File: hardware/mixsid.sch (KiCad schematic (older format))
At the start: 69 parts, among them P1 INPUT, P2 CONTROL, P4 SOCKET LEFT, P5 OUTPUT, P6 SOCKET RIGHT, Q1 BC547, Q2 BC547, U1 GAL16V8, U2 SID2, U3 7812, U4 7809, U5 SID1, U6 4052, U7 4053, U8 ICL7660

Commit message: Hardware: Replaced balance pots with round types (bourns 3339), rearranged
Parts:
- RV3, RV4: footprint Potentiometers:Potentiometer_Bourns_3296W_3-8Zoll_Inline_ScrewUp -> Potentiometers:Potentiometer_Bourns_3339P_Angular_ScrewUp
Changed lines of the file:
@@
 F 0 "RV3" H 4100 4200 50  0000 C CNN
 F 1 "10k" H 4100 4300 50  0000 C CNN
-F 2 "Potentiometers:Potentiometer_Bourns_3296W_3-8Zoll_Inline_ScrewUp" H 4100 4300 60  0001 C CNN
+F 2 "Potentiometers:Potentiometer_Bourns_3339P_Angular_ScrewUp" H 4100 4300 60  0001 C CNN
 F 3 "" H 4100 4300 60  0000 C CNN
 	1    4100 4300
@@
 F 0 "RV4" H 7050 4250 50  0000 C CNN
 F 1 "10k" H 7050 4350 50  0000 C CNN
-F 2 "Potentiometers:Potentiometer_Bourns_3296W_3-8Zoll_Inline_ScrewUp" H 7050 4350 60  0001 C CNN
+F 2 "Potentiometers:Potentiometer_Bourns_3339P_Angular_ScrewUp" H 7050 4350 60  0001 C CNN
 F 3 "" H 7050 4350 60  0000 C CNN
 	1    7050 4350

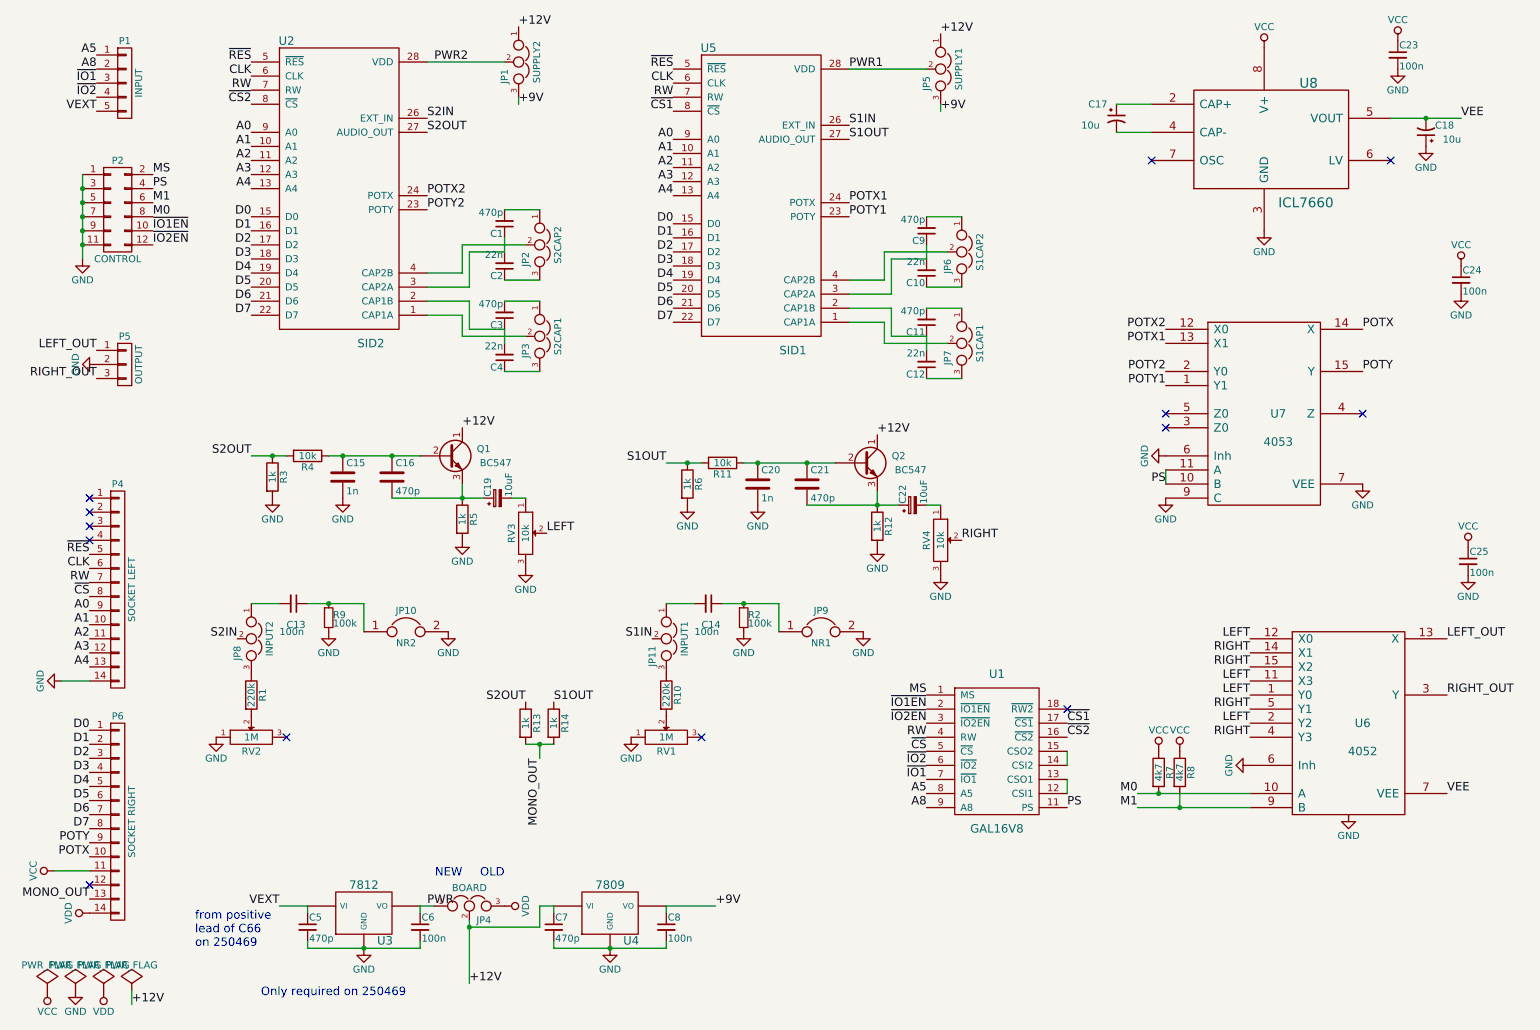
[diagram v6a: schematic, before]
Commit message: Firmware/Hardware: RW2 signal controls SID2 RW during parallel addressing
Depending on RW2, SID2 is write-only or read-write when addressed alongside
SID1.

The default setting is write-only to assure proper paddle support.
For mono tunes that use the readable registers for special effects,
parallel addressing would result in only one SID playing those effects
properly, thus RW2 allows the user to make both sids read-write.
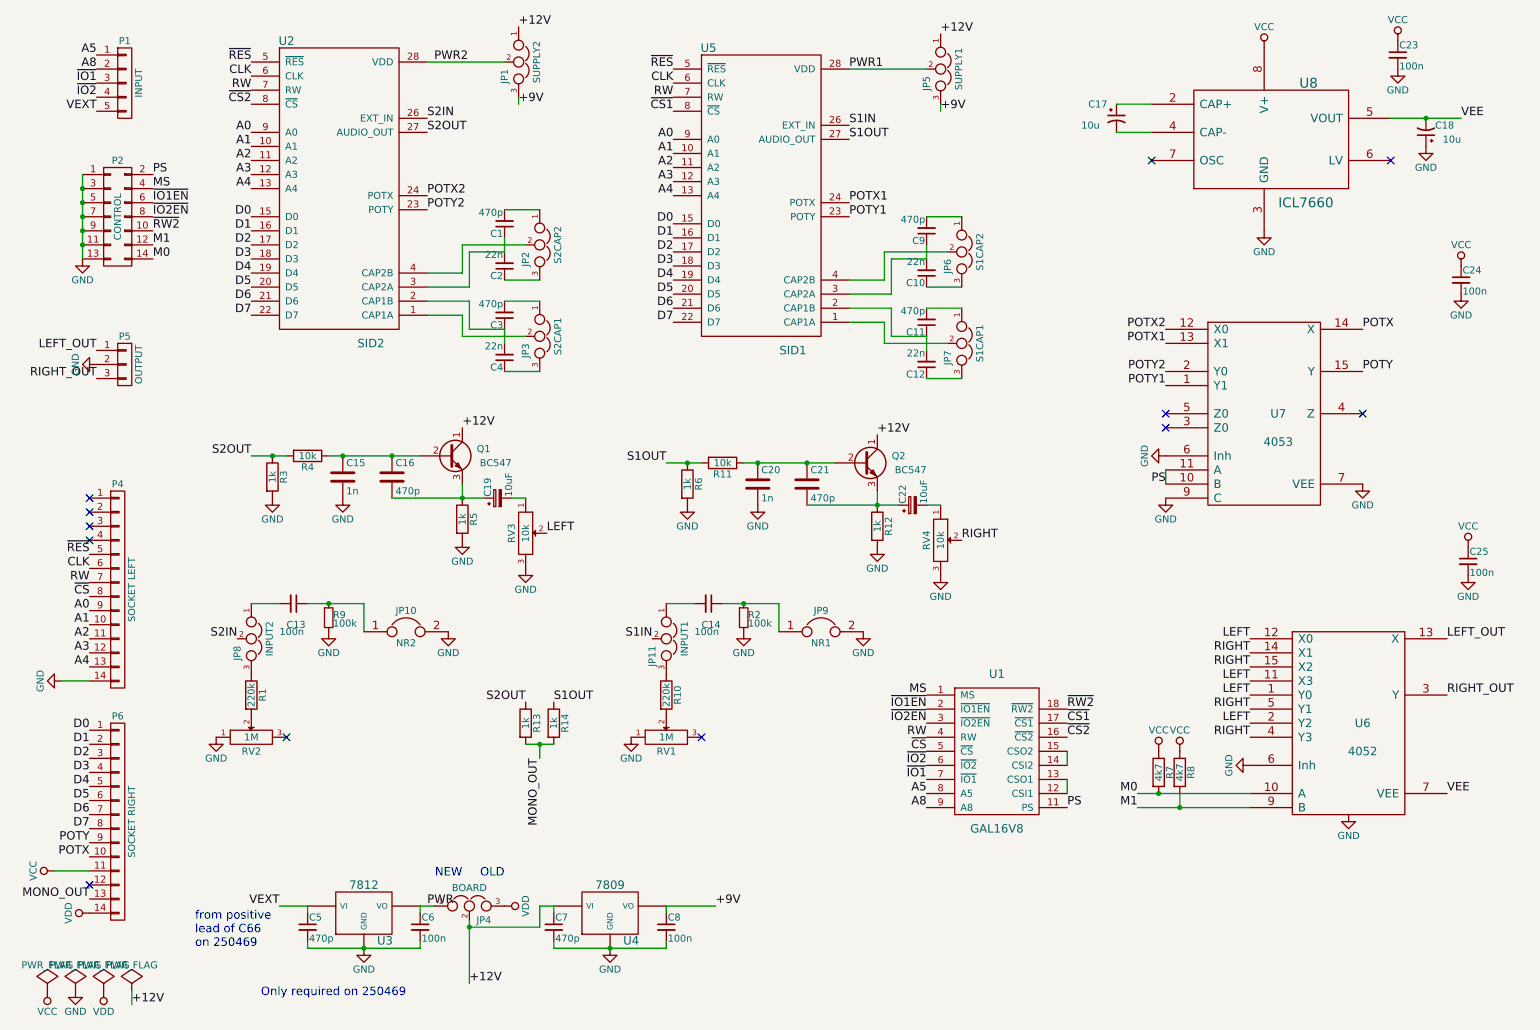
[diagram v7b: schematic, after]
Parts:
- removed P2: CONTROL, Pinheaders:Pin_Header_Straight_2x06, symbol CONN_02X06
- added P2: CONTROL, Pin_Headers:Pin_Header_Straight_2x07, symbol CONN_02X07
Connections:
- net GND: now also P2.1 (P1), P2.11 (P11), P2.13 (P13), P2.3 (P3), P2.5 (P5), P2.7 (P7), P2.9 (P9)
- net M0: now also P2.14 (P14)
- net M1: now also P2.12 (P12)
- net MS: now also P2.4 (P4)
- net PS: now also P2.2 (P2)
- net ~IO1EN: now also P2.6 (P6)
- net ~IO2EN: now also P2.8 (P8)
- net ~RW2: now reaches U1.18 (~RW2)
- net ~RW2: now also P2.10 (P10)
- no-connect marks 13 -> 12
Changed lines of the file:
@@
 Text Label 6950 5550 2    60   ~ 0
 ~IO1EN
-Text Label 1450 1750 0    60   ~ 0
+Text Label 1450 1850 0    60   ~ 0
 MS
-Text Label 1450 2150 0    60   ~ 0
+Text Label 1450 1950 0    60   ~ 0
 ~IO1EN
 $Comp
@@
 Text Label 10650 5450 0    60   ~ 0
 RIGHT_OUT
-Text Label 1450 2050 0    60   ~ 0
+Text Label 1450 2350 0    60   ~ 0
 M0
-Text Label 1450 1950 0    60   ~ 0
+Text Label 1450 2250 0    60   ~ 0
 M1
 Text Notes 3250 7600 2    60   ~ 0
@@
 Wire Wire Line
 	4200 6950 4300 6950
-Text Label 1450 2250 0    60   ~ 0
+Text Label 1450 2050 0    60   ~ 0
 ~IO2EN
 Text Label 6950 5650 2    60   ~ 0
@@
 	1    0    0    -1
 $EndComp
-NoConn ~ 7950 5550
 Text Label 7950 6250 0    60   ~ 0
 PS
@@
 Wire Wire Line
 	7950 5950 7950 5850
-$Comp
-L CONN_02X06 P2
-U 1 1 57221CBF
-P 1200 2000
-F 0 "P2" H 1200 2350 50  0000 C CNN
-F 1 "CONTROL" H 1200 1650 50  0000 C CNN
-F 2 "Pinheaders:Pin_Header_Straight_2x06" H 1200 800 60  0001 C CNN
-F 3 "" H 1200 800 60  0000 C CNN
-	1    1200 2000
-	1    0    0    -1
-$EndComp
 Connection ~ 950  2250
-Text Label 1450 1850 0    60   ~ 0
+Text Label 1450 1750 0    60   ~ 0
 PS
 $Comp
@@
 	1    0    0    -1
 $EndComp
+Text Label 7950 5550 0    60   ~ 0
+~RW2
+$Comp
+L CONN_02X07 P2
+U 1 1 57235049
+P 1200 2050
+F 0 "P2" H 1200 2450 50  0000 C CNN
+F 1 "CONTROL" V 1200 2050 50  0000 C CNN
+F 2 "Pin_Headers:Pin_Header_Straight_2x07" H 1200 850 60  0001 C CNN
+F 3 "" H 1200 850 60  0000 C CNN
+	1    1200 2050
+	1    0    0    -1
+$EndComp
+Text Label 1450 2150 0    60   ~ 0
+~RW2
 $EndSCHEMATC

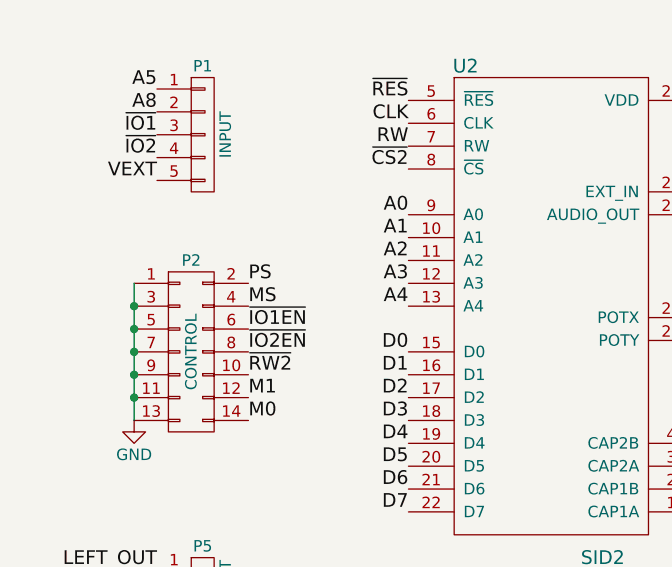
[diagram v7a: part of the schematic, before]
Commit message: Hardware: Swapped MS/PS, improved routing, silkscreen
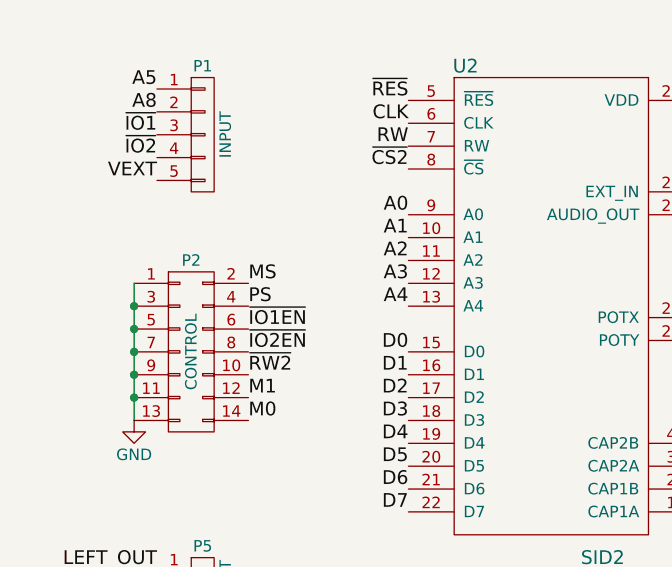
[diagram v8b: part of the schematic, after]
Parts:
- P2: footprint Pin_Headers:Pin_Header_Straight_2x07 -> Pinheaders:Pin_Header_Straight_2x07
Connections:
- net MS: now also P2.2 (P2); no longer P2.4 (P4)
- net PS: now also P2.4 (P4); no longer P2.2 (P2)
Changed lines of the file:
@@
 Text Label 6950 5550 2    60   ~ 0
 ~IO1EN
-Text Label 1450 1850 0    60   ~ 0
+Text Label 1450 1750 0    60   ~ 0
 MS
 Text Label 1450 1950 0    60   ~ 0
@@
 	7950 5950 7950 5850
 Connection ~ 950  2250
-Text Label 1450 1750 0    60   ~ 0
+Text Label 1450 1850 0    60   ~ 0
 PS
 $Comp
@@
 F 0 "P2" H 1200 2450 50  0000 C CNN
 F 1 "CONTROL" V 1200 2050 50  0000 C CNN
-F 2 "Pin_Headers:Pin_Header_Straight_2x07" H 1200 850 60  0001 C CNN
+F 2 "Pinheaders:Pin_Header_Straight_2x07" H 1200 850 60  0001 C CNN
 F 3 "" H 1200 850 60  0000 C CNN
 	1    1200 2050
